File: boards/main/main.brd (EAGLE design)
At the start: 100 x 80 mm, 28 parts, among them IC1 LSM330DLC-LGA28, IC2 PIC16(L)F1454-TSSOP-14, IC3 TPS60502-DGS, J1 RJ11-6PTH, Q1 BC547B, Q2 BC547B

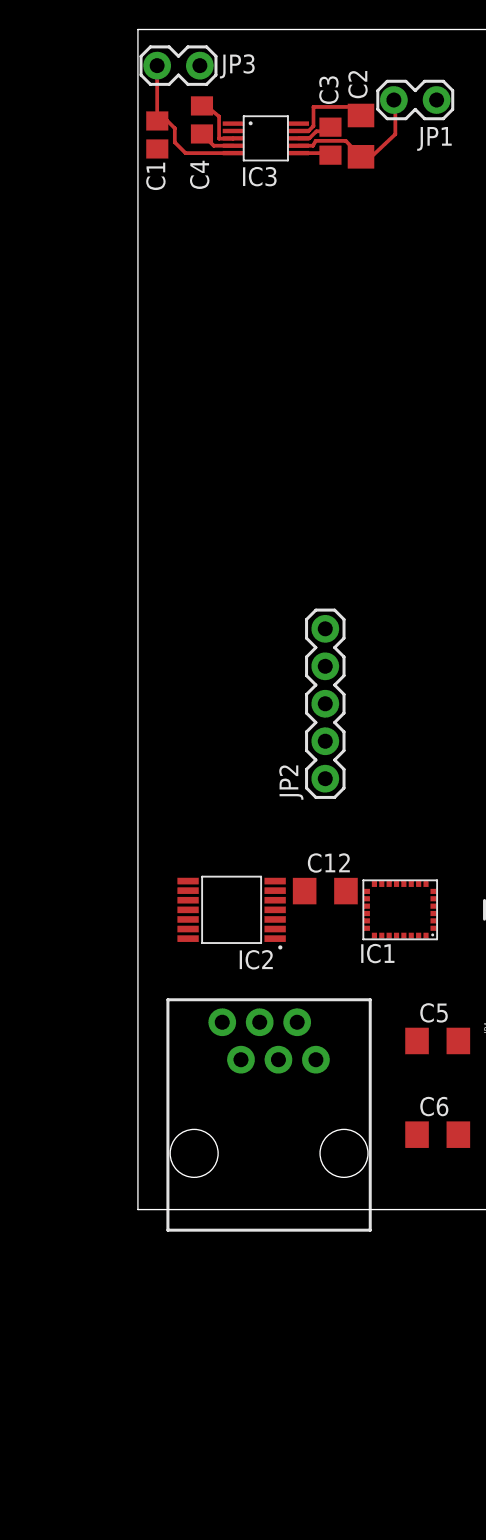
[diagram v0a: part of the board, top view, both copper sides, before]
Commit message: Added Linear Technology micropower regulator (1.8V) part and schematic.
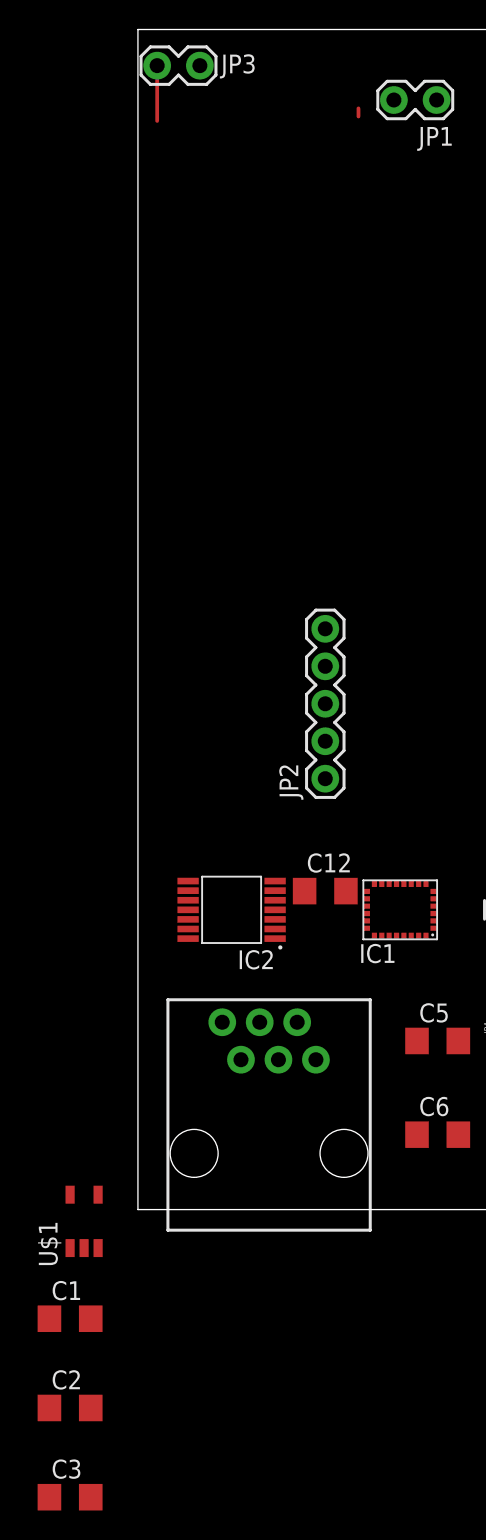
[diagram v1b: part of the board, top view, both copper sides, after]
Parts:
- removed C4: 1 uF, rcl:C0805
- removed IC3: TPS60502-DGS, leds:S-PDSO-G10
- added U$1: LT1761ES5-1.8#PBFTSOT-23, leds:TSOT-23
- C1: value 2.2 uF -> 1 uF; device rcl:C0805 -> rcl:C1206
- C2: value 10 uF -> 0.01 uF
- C3: value 1 uF -> 10 uF; device rcl:C0805 -> rcl:C1206
- moved C3 93.6 mm to (-4.60, -19.5), turned to 0 degrees
- moved C2 88.4 mm to (-4.60, -13.4), turned to 0 degrees
- moved C1 80.5 mm to (-4.60, -7.40), turned to 0 degrees
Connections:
- removed net N$3: C3.2, IC3.P$8
- removed net N$4: C4.1, IC3.P$4
- removed net N$5: C4.2, IC3.P$3
- net GND: now also C3.2, U$1.P$2; no longer C2.2, IC3.P$1, IC3.P$9
- net N$1: now also C2.2, C3.1, U$1.P$5; no longer C2.1, IC3.P$10, IC3.P$7, JP1.2
- net N$2: now also C2.1, U$1.P$4; no longer C3.1, IC3.P$6
- net VDD: now also JP1.2, U$1.P$1, U$1.P$3; no longer IC3.P$5
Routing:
- net N$1: track 10.3 -> 0.00 mm
- net VDD: track 10.4 -> 3.75 mm
- net GND: track 6.14 -> 0.00 mm
- net N$5: track 3.90 -> 0.00 mm
- net N$4: track 2.46 -> 0.00 mm
- net N$3: track 2.44 -> 0.00 mm
- net N$2: track 2.23 -> 0.00 mm

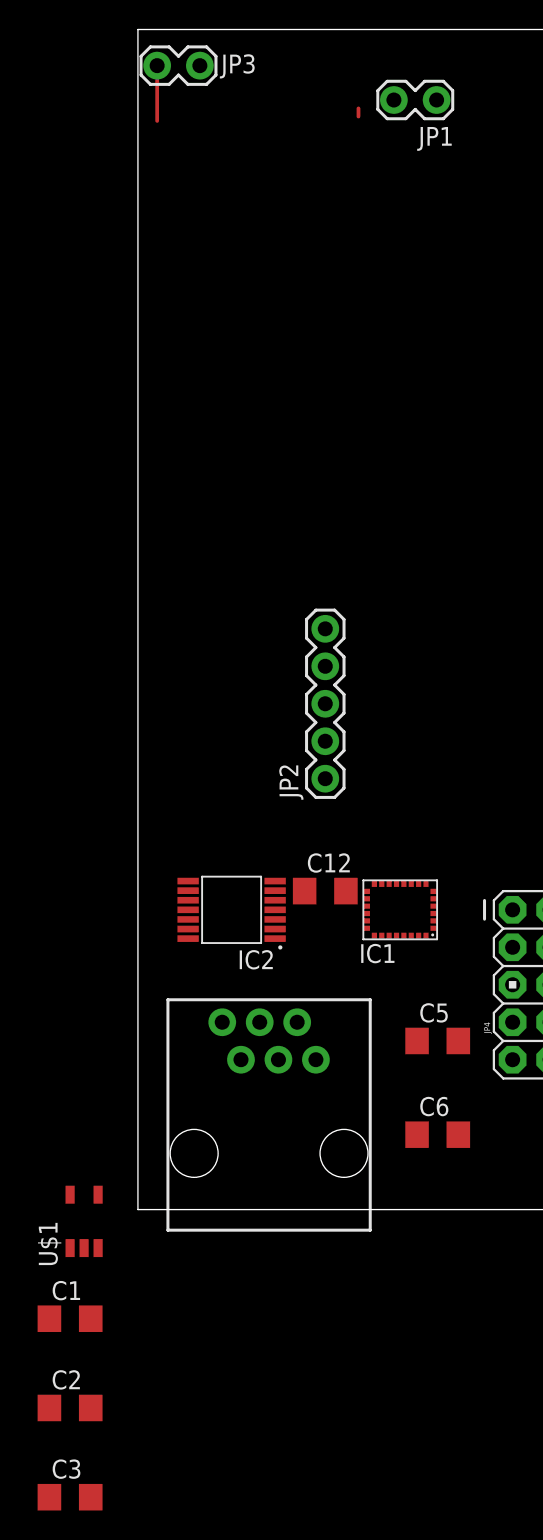
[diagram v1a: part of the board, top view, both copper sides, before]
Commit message: Added regulator to layout.
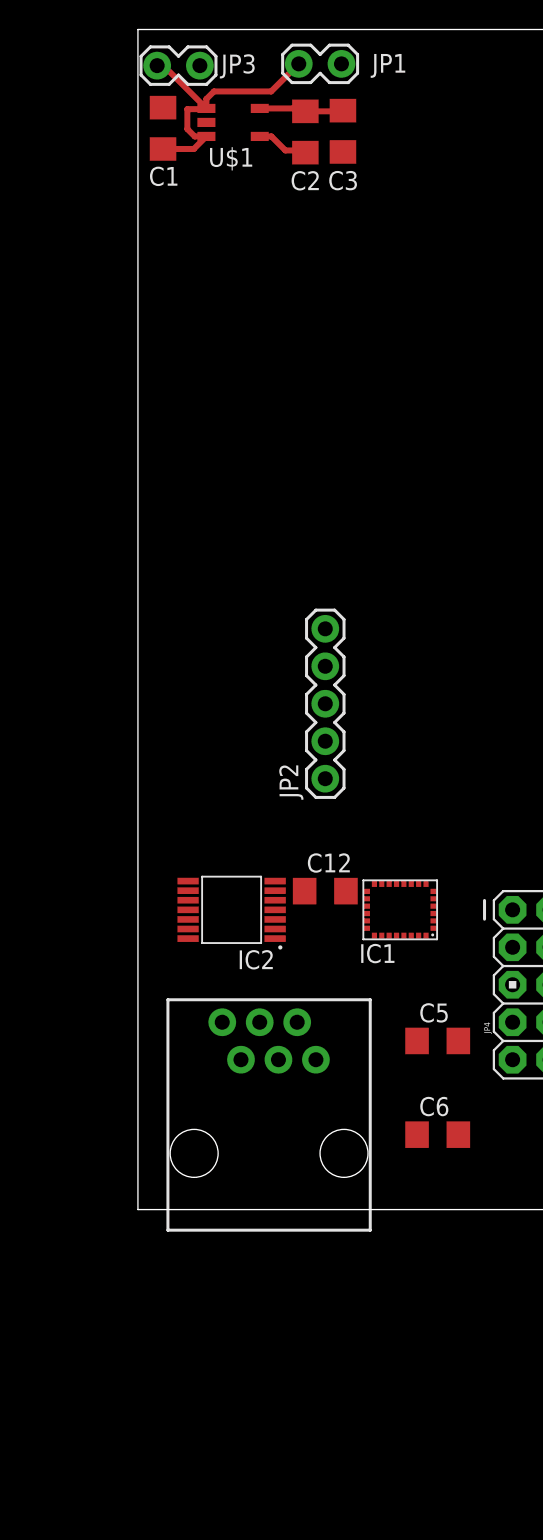
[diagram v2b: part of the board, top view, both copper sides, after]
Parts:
- moved C3 94.4 mm to (13.9, 73.1), turned to 270 degrees
- moved C2 88.0 mm to (11.3, 73.0), turned to 90 degrees
- moved C1 80.9 mm to (1.70, 73.3), turned to 90 degrees
- moved U$1 75.2 mm to (6.45, 73.7), turned to 270 degrees
- moved JP1 6.90 mm to (13.6, 77.7)
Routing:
- net VDD: track 3.75 -> 19.9 mm
- net N$1: track 0.00 -> 5.67 mm
- net N$2: track 0.00 -> 3.55 mm
- net N$32: track 0.55 -> 0.00 mm
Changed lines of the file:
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@@
 <element name="IC2" library="leds" package="TSSOP-14" value="PIC16(L)F1454-TSSOP-14" x="6.35" y="20.32" rot="R180"/>
 <element name="J1" library="SparkFun-Connectors" package="RJ11-6" value="RJ11-6PTH" x="3.81" y="3.81"/>
-<element name="JP1" library="SparkFun-Connectors" package="1X02_LOCK" value="M02LOCK" x="20.07" y="75.22" rot="R180"/>
+<element name="JP1" library="SparkFun-Connectors" package="1X02_LOCK" value="M02LOCK" x="13.62" y="77.67" smashed="yes" rot="R180">
+<attribute name="NAME" x="18.2662" y="78.3412" size="1.27" layer="25" ratio="10" rot="R180"/>
+<attribute name="VALUE" x="14.89" y="80.845" size="1.27" layer="27" rot="R180"/>
+</element>
 <element name="C5" library="rcl" package="C1206" value=".1 uF" x="20.32" y="11.43"/>
 <element name="C6" library="rcl" package="C1206" value=".1 uF" x="20.32" y="5.08"/>
@@
 <attribute name="VALUE" x="0.21" y="74.375" size="1.27" layer="27"/>
 </element>
-<element name="U$1" library="leds" package="TSOT-23" value="LT1761ES5-1.8#PBFTSOT-23" x="-3.65" y="-0.8"/>
-<element name="C1" library="rcl" package="C1206" value="1 uF" x="-4.6" y="-7.4"/>
-<element name="C2" library="rcl" package="C1206" value="0.01 uF" x="-4.6" y="-13.45"/>
-<element name="C3" library="rcl" package="C1206" value="10 uF" x="-4.6" y="-19.5"/>
+<element name="U$1" library="leds" package="TSOT-23" value="LT1761ES5-1.8#PBFTSOT-23" x="6.45" y="73.7" smashed="yes" rot="R270">
+<attribute name="NAME" x="4.75" y="70.7" size="1.27" layer="25"/>
+<attribute name="VALUE" x="3.35" y="70.6" size="1.27" layer="27"/>
+</element>
+<element name="C1" library="rcl" package="C1206" value="1 uF" x="1.7" y="73.3" smashed="yes" rot="R90">
+<attribute name="NAME" x="2.82" y="70.68" size="1.27" layer="25" rot="R180"/>
+<attribute name="VALUE" x="4.24" y="72.03" size="1.27" layer="27" rot="R90"/>
+</element>
+<element name="C2" library="rcl" package="C1206" value="0.01 uF" x="11.35" y="73.05" smashed="yes" rot="R90">
+<attribute name="NAME" x="12.42" y="70.38" size="1.27" layer="25" rot="R180"/>
+<attribute name="VALUE" x="13.89" y="71.78" size="1.27" layer="27" rot="R90"/>
+</element>
+<element name="C3" library="rcl" package="C1206" value="10 uF" x="13.9" y="73.1" smashed="yes" rot="R270">
+<attribute name="NAME" x="12.88" y="69.12" size="1.27" layer="25"/>
+<attribute name="VALUE" x="11.36" y="74.37" size="1.27" layer="27" rot="R270"/>
+</element>
 </elements>
 <signals>
@@
 <wire x1="50.8" y1="62.23" x2="63.63" y2="62.23" width="0" layer="19" extent="1-1"/>
 <wire x1="50.8" y1="57.15" x2="50.8" y2="62.23" width="0" layer="19" extent="1-1"/>
+<wire x1="13.9" y1="71.7" x2="50.8" y2="62.23" width="0" layer="19" extent="1-1"/>
+<wire x1="4.64" y1="73.7" x2="13.9" y2="71.7" width="0" layer="19" extent="1-1"/>
+<wire x1="1.7" y1="74.7" x2="4.64" y2="73.7" width="0" layer="19" extent="1-1"/>
+<wire x1="4.1978" y1="77.55" x2="1.7" y2="74.7" width="0" layer="19" extent="1-1"/>
 <wire x1="20.0425" y1="21.57" x2="63.63" y2="36.83" width="0" layer="19" extent="1-1"/>
 <wire x1="20.0425" y1="21.07" x2="20.0425" y2="21.57" width="0" layer="19" extent="1-1"/>
@@
 <wire x1="8.255" y1="12.7" x2="14.1" y2="21.59" width="0" layer="19" extent="1-1"/>
 <wire x1="3.4" y1="18.37" x2="8.255" y2="12.7" width="0" layer="19" extent="1-1"/>
-<wire x1="-3.65" y1="-2.61" x2="8.255" y2="12.7" width="0" layer="19" extent="1-1"/>
-<wire x1="-3.2" y1="-7.4" x2="-3.65" y2="-2.61" width="0" layer="19" extent="1-1"/>
-<wire x1="-3.2" y1="-19.5" x2="-3.2" y2="-7.4" width="0" layer="19" extent="1-1"/>
-<wire x1="4.1978" y1="77.55" x2="50.8" y2="62.23" width="0" layer="19" extent="1-1"/>
 </signal>
 <signal name="VDD">
@@
 <contactref element="IC1" pad="P$10"/>
 <contactref element="JP3" pad="1"/>
-<wire x1="1.3022" y1="73.8" x2="1.3022" y2="77.55" width="0.254" layer="1"/>
 <contactref element="JP1" pad="2"/>
 <contactref element="C1" pad="1"/>
 <contactref element="U$1" pad="P$1"/>
 <contactref element="U$1" pad="P$3"/>
+<wire x1="1.3022" y1="77.55" x2="1.74" y2="77.55" width="0.4064" layer="1"/>
+<wire x1="1.74" y1="77.55" x2="4.64" y2="74.65" width="0.4064" layer="1"/>
+<wire x1="1.7" y1="71.9" x2="3.79" y2="71.9" width="0.4064" layer="1"/>
+<wire x1="3.79" y1="71.9" x2="4.64" y2="72.75" width="0.4064" layer="1"/>
+<wire x1="4.64" y1="72.75" x2="3.85" y2="72.75" width="0.4064" layer="1"/>
+<wire x1="3.85" y1="72.75" x2="3.35" y2="73.25" width="0.4064" layer="1"/>
+<wire x1="3.35" y1="73.25" x2="3.35" y2="74.6" width="0.4064" layer="1"/>
+<wire x1="3.35" y1="74.6" x2="4.59" y2="74.6" width="0.4064" layer="1"/>
+<wire x1="4.59" y1="74.6" x2="4.64" y2="74.65" width="0.4064" layer="1"/>
+<wire x1="4.64" y1="74.65" x2="4.64" y2="75.29" width="0.4064" layer="1"/>
+<wire x1="4.64" y1="75.29" x2="5.15" y2="75.8" width="0.4064" layer="1"/>
+<wire x1="5.15" y1="75.8" x2="9.0322" y2="75.8" width="0.4064" layer="1"/>
+<wire x1="9.0322" y1="75.8" x2="10.9022" y2="77.67" width="0.4064" layer="1"/>
 <wire x1="60.83" y1="43.18" x2="60.83" y2="49.53" width="0" layer="19" extent="1-1"/>
 <wire x1="60.83" y1="36.83" x2="60.83" y2="43.18" width="0" layer="19" extent="1-1"/>
@@
 <wire x1="16.53" y1="22.0825" x2="17.03" y2="22.0825" width="0" layer="19" extent="1-1"/>
 <wire x1="16.03" y1="22.0825" x2="16.53" y2="22.0825" width="0" layer="19" extent="1-1"/>
-<wire x1="-2.7" y1="-2.61" x2="16.03" y2="22.0825" width="0" layer="19" extent="1-1"/>
-<wire x1="-4.6" y1="-2.61" x2="-2.7" y2="-2.61" width="0" layer="19" extent="1-1"/>
-<wire x1="-6" y1="-7.4" x2="-4.6" y2="-2.61" width="0" layer="19" extent="1-1"/>
-<wire x1="17.3522" y1="75.22" x2="48.26" y2="52.07" width="0" layer="19" extent="1-1"/>
-<wire x1="1.3022" y1="73.8" x2="17.3522" y2="75.22" width="0" layer="19" extent="1-1"/>
+<wire x1="10.9022" y1="77.67" x2="48.26" y2="52.07" width="0" layer="19" extent="1-1"/>
 </signal>
 <signal name="N$1">
@@
 <contactref element="C2" pad="2"/>
 <contactref element="C3" pad="1"/>
+<wire x1="8.26" y1="74.65" x2="10.5" y2="74.65" width="0.4064" layer="1"/>
+<wire x1="10.5" y1="74.65" x2="11.35" y2="74.45" width="0.4064" layer="1"/>
+<wire x1="11.35" y1="74.45" x2="13.35" y2="74.45" width="0.4064" layer="1"/>
+<wire x1="13.35" y1="74.45" x2="13.9" y2="74.5" width="0.4064" layer="1"/>
 <wire x1="60.83" y1="55.88" x2="60.83" y2="62.23" width="0" layer="19" extent="1-1"/>
-<wire x1="18.03" y1="18.5575" x2="60.83" y2="55.88" width="0" layer="19" extent="1-1"/>
-<wire x1="16.03" y1="18.5575" x2="18.03" y2="18.5575" width="0" layer="19" extent="1-1"/>
-<wire x1="-4.6" y1="1.01" x2="16.03" y2="18.5575" width="0" layer="19" extent="1-1"/>
-<wire x1="-3.2" y1="-13.45" x2="-4.6" y2="1.01" width="0" layer="19" extent="1-1"/>
-<wire x1="-6" y1="-19.5" x2="-3.2" y2="-13.45" width="0" layer="19" extent="1-1"/>
+<wire x1="13.9" y1="74.5" x2="60.83" y2="62.23" width="0" layer="19" extent="1-1"/>
+<wire x1="16.03" y1="18.5575" x2="13.35" y2="74.45" width="0" layer="19" extent="1-1"/>
+<wire x1="18.03" y1="18.5575" x2="16.03" y2="18.5575" width="0" layer="19" extent="1-1"/>
 </signal>
 <signal name="N$6">
@@
 <contactref element="IC2" pad="P$11"/>
 <contactref element="C6" pad="1"/>
-<wire x1="3.4" y1="20.32" x2="20.2478" y2="75.22" width="0" layer="19" extent="1-1"/>
+<wire x1="3.4" y1="20.32" x2="13.7978" y2="77.67" width="0" layer="19" extent="1-1"/>
 <wire x1="9.3" y1="18.37" x2="3.4" y2="20.32" width="0" layer="19" extent="1-1"/>
 <wire x1="6.985" y1="10.16" x2="9.3" y2="18.37" width="0" layer="19" extent="1-1"/>
@@
 <signal name="N$31">
 </signal>
-<signal name="N$32">
-<wire x1="14.95" y1="74.65" x2="14.95" y2="74.1" width="0.254" layer="1"/>
-</signal>
 <signal name="N$26">
 </signal>
@@
 <contactref element="U$1" pad="P$4"/>
 <contactref element="C2" pad="1"/>
-<wire x1="-2.7" y1="1.01" x2="-6" y2="-13.45" width="0" layer="19" extent="1-1"/>
+<wire x1="8.26" y1="72.75" x2="9.05" y2="72.75" width="0.4064" layer="1"/>
+<wire x1="9.05" y1="72.75" x2="10" y2="71.8" width="0.4064" layer="1"/>
+<wire x1="10" y1="71.8" x2="11.2" y2="71.8" width="0.4064" layer="1"/>
+<wire x1="11.2" y1="71.8" x2="11.35" y2="71.65" width="0.4064" layer="1"/>
 </signal>
 </signals>
